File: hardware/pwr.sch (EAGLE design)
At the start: 21 parts, among them IC2 LM2675M-ADJ, Q2 IRFR5305, T1 BC846, T2 BC846, X3 MKDSN1,5/4-5,08

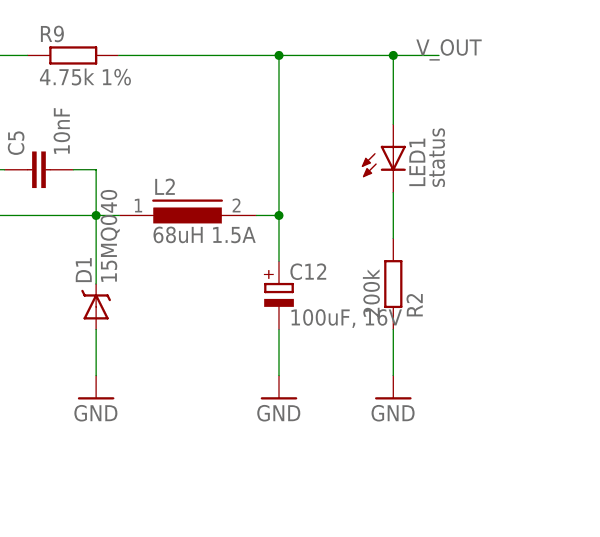
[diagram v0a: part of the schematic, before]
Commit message: pwr board  width decrease
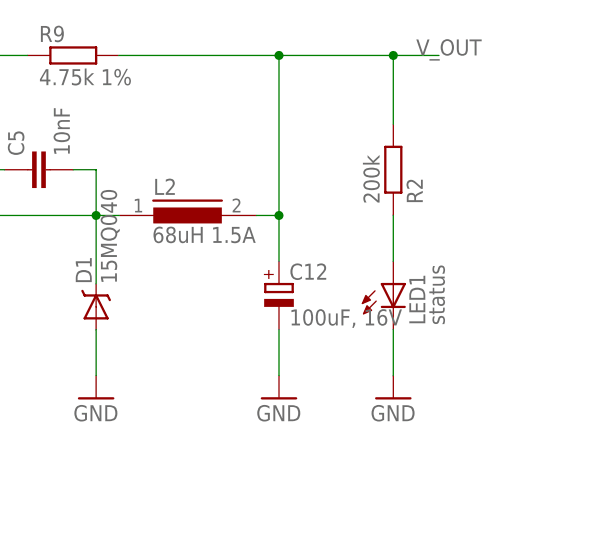
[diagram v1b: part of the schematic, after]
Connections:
- net GND: now also LED1.C; no longer R2.1
- net N$1: now also LED1.A, R2.1; no longer LED1.C, R2.2
- net V_OUT: now also R2.2; no longer LED1.A
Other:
- moved on the sheet: LED1, R2
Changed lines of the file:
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@@
 <instance part="R31" gate="G$1" x="248.92" y="68.58" rot="MR180"/>
 <instance part="Q2" gate="G$1" x="309.88" y="104.14" rot="R90"/>
-<instance part="LED1" gate="G$1" x="403.86" y="116.84"/>
-<instance part="R2" gate="G$1" x="403.86" y="101.6" rot="MR90"/>
+<instance part="LED1" gate="G$1" x="403.86" y="101.6"/>
+<instance part="R2" gate="G$1" x="403.86" y="114.3" rot="MR90"/>
 <instance part="GND1" gate="1" x="403.86" y="88.9"/>
 <instance part="GND2" gate="1" x="299.72" y="5.08"/>
@@
 </segment>
 <segment>
-<pinref part="R2" gate="G$1" pin="1"/>
-<pinref part="GND1" gate="1" pin="GND"/>
-<wire x1="403.86" y1="96.52" x2="403.86" y2="91.44" width="0.1524" layer="91"/>
-</segment>
-<segment>
 <pinref part="X3" gate="-1" pin="KL"/>
 <pinref part="GND2" gate="1" pin="GND"/>
@@
 <pinref part="GND6" gate="1" pin="GND"/>
 <wire x1="292.1" y1="63.5" x2="292.1" y2="58.42" width="0.1524" layer="91"/>
+</segment>
+<segment>
+<pinref part="GND1" gate="1" pin="GND"/>
+<pinref part="LED1" gate="G$1" pin="C"/>
+<wire x1="403.86" y1="91.44" x2="403.86" y2="96.52" width="0.1524" layer="91"/>
 </segment>
 </net>
@@
 </segment>
 </net>
-<net name="N$1" class="0">
-<segment>
-<pinref part="LED1" gate="G$1" pin="C"/>
-<pinref part="R2" gate="G$1" pin="2"/>
-<wire x1="403.86" y1="111.76" x2="403.86" y2="106.68" width="0.1524" layer="91"/>
-</segment>
-</net>
 <net name="V_IN" class="0">
 <segment>
@@
 <wire x1="391.16" y1="127" x2="403.86" y2="127" width="0.1524" layer="91"/>
 <junction x="391.16" y="127"/>
-<pinref part="LED1" gate="G$1" pin="A"/>
+<label x="406.4" y="127" size="1.778" layer="95"/>
+<pinref part="R2" gate="G$1" pin="2"/>
+<wire x1="403.86" y1="127" x2="408.94" y2="127" width="0.1524" layer="91"/>
 <wire x1="403.86" y1="119.38" x2="403.86" y2="127" width="0.1524" layer="91"/>
-<wire x1="403.86" y1="127" x2="408.94" y2="127" width="0.1524" layer="91"/>
 <junction x="403.86" y="127"/>
-<label x="406.4" y="127" size="1.778" layer="95"/>
 </segment>
 </net>
@@
 </segment>
 </net>
+<net name="N$1" class="0">
+<segment>
+<pinref part="LED1" gate="G$1" pin="A"/>
+<pinref part="R2" gate="G$1" pin="1"/>
+<wire x1="403.86" y1="104.14" x2="403.86" y2="109.22" width="0.1524" layer="91"/>
+</segment>
+</net>

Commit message: board ready
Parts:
- removed C1: 10nF, rcl:C-EUC0805
- removed Q2: IRFR5305, transistor-power:IRFR5305
- removed R4: 220k, rcl:R-EU_R0805W
- removed R9: 4.75k 1%, rcl:R-EU_R0805W
- removed T2: BC846, transistor:BC846
- added R10: 200k, rcl:R-EU_R0805W
- IC1: value LM2675M-ADJ -> (none)
- R2: value 200k -> 4k
- renumbered IC2 to IC1
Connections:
- removed net N$16: C1.1, Q2.G, R4.1, T2.C
- removed net N$5: Q2.S, R3.2, R4.2, U$1.P$2
- net CE: now also X3-3.KL; no longer X3-4.KL
- net GND: now also IC1G$1.GND, X3-4.KL; no longer IC1.GND, T2.E, X3-1.KL
- net N$1: now also R10.1; no longer R2.1
- net N$10: now also IC1G$1.CB; no longer IC1.CB
- net N$2: now also IC1G$1.ON/OFF; no longer T2.B
- net N$4: now also IC1G$1.FB, R2.1; no longer IC1.FB, R9.1
- net N$49: now also IC1G$1.VIN, R3.2, U$1.P$2; no longer C1.2, IC1.VIN, Q2.D
- net N$9: now also IC1G$1.VSW; no longer IC1.VSW
- net V_IN: now also X3-1.KL; no longer X3-3.KL
- net V_OUT: now also R10.2; no longer R9.2
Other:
- note added: "Vout=1.21(1+R2/R1)"
- moved on the sheet: C12, C2, D1, R2, R3, R31, R5, T1
